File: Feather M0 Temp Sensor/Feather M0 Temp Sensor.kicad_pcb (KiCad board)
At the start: 2 copper layers, 35.6 x 22.9 mm, 3 parts, among them J1 Feather_Long_Side, J2 Feather_Short_Side, U1 Adafruit_SHT4x

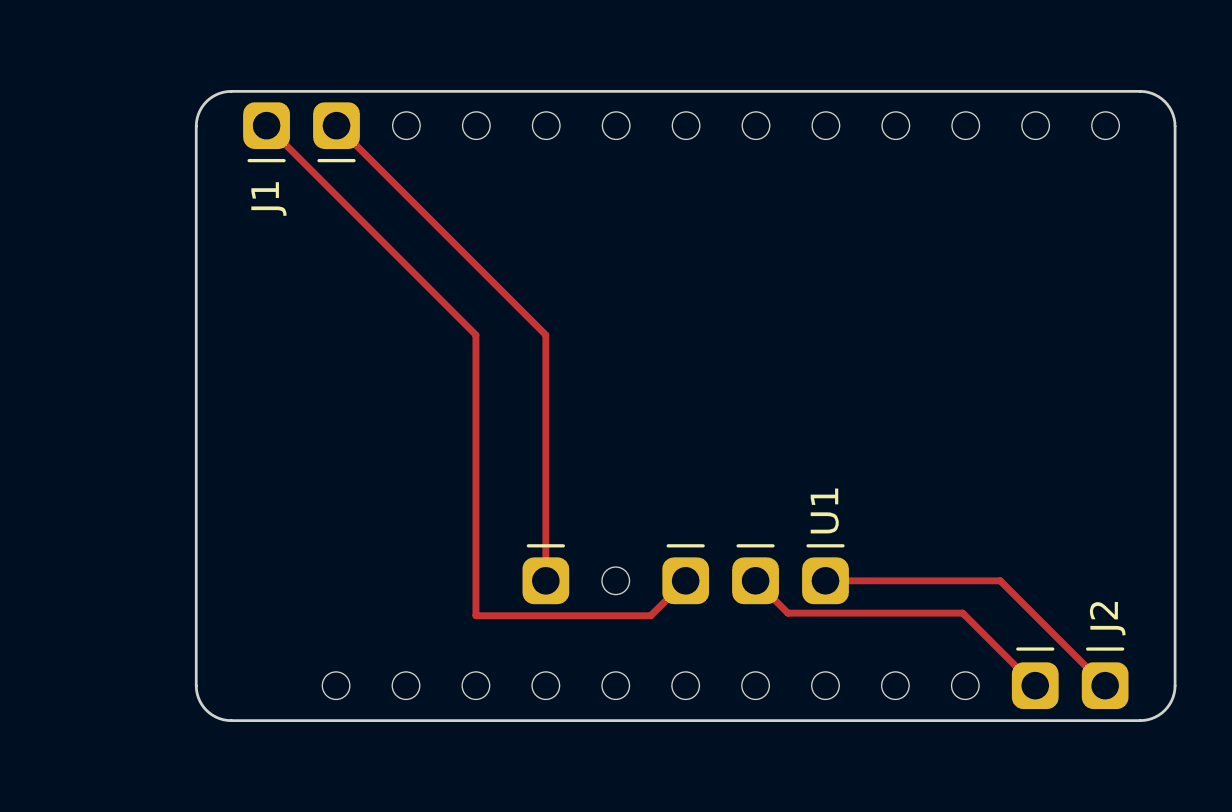
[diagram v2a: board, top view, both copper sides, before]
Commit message: Finalised PCB
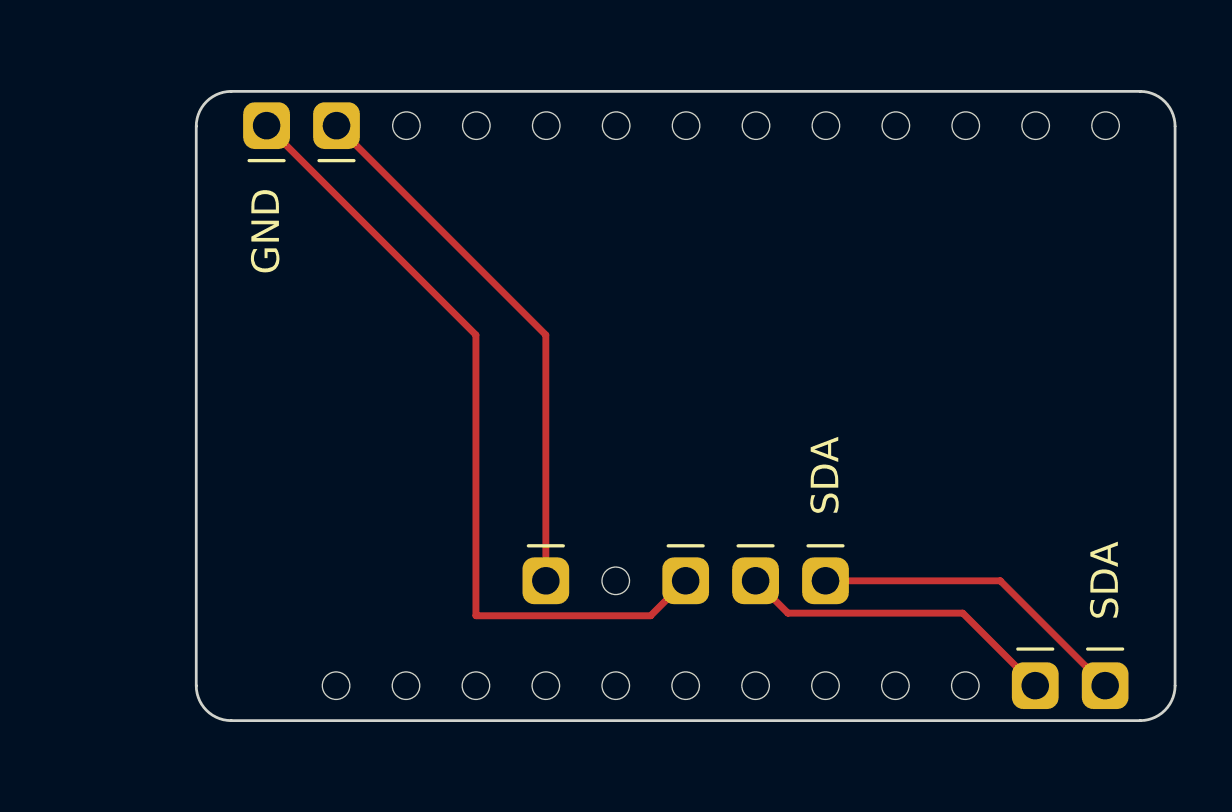
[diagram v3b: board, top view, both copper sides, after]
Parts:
- renumbered J1 to GND, U1 to SDA, J2 to SDA
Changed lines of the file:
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@@
     (property "Sheetname" "")
     (attr through_hole)
-    (fp_text reference "J1" (at -2.565 -0.015 90) (layer "F.SilkS")
+    (fp_text reference "GND" (at -3.835 -0.015 90) (layer "F.SilkS")
       (effects (font (size 1 1) (thickness 0.15)))
     )
@@
     (fp_line (start 1.75 32.25) (end -1.8 32.25) (layer "F.CrtYd") (width 0.05))
     (fp_line (start 1.75 -1.8) (end 1.75 32.25) (layer "F.CrtYd") (width 0.05))
+    (pad "" thru_hole oval (at 0 25.4 90) (size 1.7 1.7) (drill 1) (layers *.Mask)
+      (pinfunction "Pin_11") (pintype "passive"))
+    (pad "" thru_hole oval (at 0 15.24 90) (size 1.7 1.7) (drill 1) (layers *.Mask)
+      (pinfunction "Pin_7") (pintype "passive"))
+    (pad "" thru_hole oval (at 0 27.94 90) (size 1.7 1.7) (drill 1) (layers *.Mask)
+      (pinfunction "Pin_12") (pintype "passive"))
+    (pad "" thru_hole oval (at 0 30.48 90) (size 1.7 1.7) (drill 1) (layers *.Mask)
+      (pinfunction "Pin_13") (pintype "passive"))
+    (pad "" thru_hole oval (at 0 12.7 90) (size 1.7 1.7) (drill 1) (layers *.Mask)
+      (pinfunction "Pin_6") (pintype "passive"))
+    (pad "" thru_hole oval (at 0 22.86 90) (size 1.7 1.7) (drill 1) (layers *.Mask)
+      (pinfunction "Pin_10") (pintype "passive"))
+    (pad "" thru_hole oval (at 0 5.08 90) (size 1.7 1.7) (drill 1) (layers *.Mask)
+      (pinfunction "Pin_3") (pintype "passive"))
+    (pad "" thru_hole oval (at 0 7.62 90) (size 1.7 1.7) (drill 1) (layers *.Mask)
+      (pinfunction "Pin_4") (pintype "passive"))
+    (pad "" thru_hole oval (at 0 17.78 90) (size 1.7 1.7) (drill 1) (layers *.Mask)
+      (pinfunction "Pin_8") (pintype "passive"))
+    (pad "" thru_hole oval (at 0 20.32 90) (size 1.7 1.7) (drill 1) (layers *.Mask)
+      (pinfunction "Pin_9") (pintype "passive"))
+    (pad "" thru_hole oval (at 0 10.16 90) (size 1.7 1.7) (drill 1) (layers *.Mask)
+      (pinfunction "Pin_5") (pintype "passive"))
     (pad "1" thru_hole roundrect (at 0 0 90) (size 1.7 1.7) (drill 1) (layers *.Cu *.Mask) (roundrect_rratio 0.25)
       (net 2 "Net-(U1-Pad3)") (pinfunction "GND") (pintype "power_out"))
     (pad "2" thru_hole roundrect (at 0 2.54 90) (size 1.7 1.7) (drill 1) (layers *.Cu *.Mask) (roundrect_rratio 0.25)
       (net 3 "Net-(U1-Pad5)") (pinfunction "A0") (pintype "power_out"))
-    (pad "3" thru_hole oval (at 0 5.08 90) (size 1.7 1.7) (drill 1) (layers *.Mask)
-      (pinfunction "Pin_3") (pintype "passive"))
-    (pad "4" thru_hole oval (at 0 7.62 90) (size 1.7 1.7) (drill 1) (layers *.Mask)
-      (pinfunction "Pin_4") (pintype "passive"))
-    (pad "5" thru_hole oval (at 0 10.16 90) (size 1.7 1.7) (drill 1) (layers *.Mask)
-      (pinfunction "Pin_5") (pintype "passive"))
-    (pad "6" thru_hole oval (at 0 12.7 90) (size 1.7 1.7) (drill 1) (layers *.Mask)
-      (pinfunction "Pin_6") (pintype "passive"))
-    (pad "7" thru_hole oval (at 0 15.24 90) (size 1.7 1.7) (drill 1) (layers *.Mask)
-      (pinfunction "Pin_7") (pintype "passive"))
-    (pad "8" thru_hole oval (at 0 17.78 90) (size 1.7 1.7) (drill 1) (layers *.Mask)
-      (pinfunction "Pin_8") (pintype "passive"))
-    (pad "9" thru_hole oval (at 0 20.32 90) (size 1.7 1.7) (drill 1) (layers *.Mask)
-      (pinfunction "Pin_9") (pintype "passive"))
-    (pad "10" thru_hole oval (at 0 22.86 90) (size 1.7 1.7) (drill 1) (layers *.Mask)
-      (pinfunction "Pin_10") (pintype "passive"))
-    (pad "11" thru_hole oval (at 0 25.4 90) (size 1.7 1.7) (drill 1) (layers *.Mask)
-      (pinfunction "Pin_11") (pintype "passive"))
-    (pad "12" thru_hole oval (at 0 27.94 90) (size 1.7 1.7) (drill 1) (layers *.Mask)
-      (pinfunction "Pin_12") (pintype "passive"))
-    (pad "13" thru_hole oval (at 0 30.48 90) (size 1.7 1.7) (drill 1) (layers *.Mask)
-      (pinfunction "Pin_13") (pintype "passive"))
     (model "${KICAD6_3DMODEL_DIR}/Connector_PinSocket_2.54mm.3dshapes/PinSocket_1x13_P2.54mm_Vertical.wrl"
       (offset (xyz 0 0 0))
@@
     (property "Sheetname" "")
     (attr through_hole)
-    (fp_text reference "U1" (at -2.54 0 90) (layer "F.SilkS")
+    (fp_text reference "SDA" (at -3.81 0 90) (layer "F.SilkS")
       (effects (font (size 1 1) (thickness 0.15)))
     )
@@
     (fp_line (start 1.75 11.9) (end -1.8 11.9) (layer "F.CrtYd") (width 0.05))
     (fp_line (start -1.8 -1.8) (end 1.75 -1.8) (layer "F.CrtYd") (width 0.05))
+    (pad "" thru_hole oval (at 0 7.62 270) (size 1.7 1.7) (drill 1) (layers *.Mask)
+      (pinfunction "3V") (pintype "power_out"))
     (pad "1" thru_hole roundrect (at 0 0 270) (size 1.7 1.7) (drill 1) (layers *.Cu *.Mask) (roundrect_rratio 0.25)
       (net 1 "Net-(J2-Pad1)") (pinfunction "SDA") (pintype "bidirectional"))
@@
     (pad "3" thru_hole roundrect (at 0 5.08 270) (size 1.7 1.7) (drill 1) (layers *.Cu *.Mask) (roundrect_rratio 0.25)
       (net 2 "Net-(U1-Pad3)") (pinfunction "GND") (pintype "power_in"))
-    (pad "4" thru_hole oval (at 0 7.62 270) (size 1.7 1.7) (drill 1) (layers *.Mask)
-      (pinfunction "3V") (pintype "power_out"))
     (pad "5" thru_hole roundrect (at 0 10.16 270) (size 1.7 1.7) (drill 1) (layers *.Cu *.Mask) (roundrect_rratio 0.25)
       (net 3 "Net-(U1-Pad5)") (pinfunction "VIN") (pintype "power_in"))
@@
     (property "Sheetname" "")
     (attr through_hole)
-    (fp_text reference "J2" (at -2.54 0 90) (layer "F.SilkS")
+    (fp_text reference "SDA" (at -3.81 0 90) (layer "F.SilkS")
       (effects (font (size 1 1) (thickness 0.15)))
     )
@@
     (fp_line (start 1.75 -1.8) (end 1.75 29.7) (layer "F.CrtYd") (width 0.05))
     (fp_line (start 1.75 29.7) (end -1.8 29.7) (layer "F.CrtYd") (width 0.05))
+    (pad "" thru_hole oval (at 0 17.78 270) (size 1.7 1.7) (drill 1) (layers *.Mask)
+      (pinfunction "Pin_8") (pintype "passive"))
+    (pad "" thru_hole oval (at 0 7.62 270) (size 1.7 1.7) (drill 1) (layers *.Mask)
+      (pinfunction "Pin_4") (pintype "passive"))
+    (pad "" thru_hole oval (at 0 10.16 270) (size 1.7 1.7) (drill 1) (layers *.Mask)
+      (pinfunction "Pin_5") (pintype "passive"))
+    (pad "" thru_hole oval (at 0 5.08 270) (size 1.7 1.7) (drill 1) (layers *.Mask)
+      (pinfunction "Pin_3") (pintype "passive"))
+    (pad "" thru_hole oval (at 0 12.7 270) (size 1.7 1.7) (drill 1) (layers *.Mask)
+      (pinfunction "Pin_6") (pintype "passive"))
+    (pad "" thru_hole oval (at 0 20.32 270) (size 1.7 1.7) (drill 1) (layers *.Mask)
+      (pinfunction "Pin_9") (pintype "passive"))
+    (pad "" thru_hole oval (at 0 25.4 270) (size 1.7 1.7) (drill 1) (layers *.Mask)
+      (pinfunction "Pin_11") (pintype "passive"))
+    (pad "" thru_hole oval (at 0 15.24 270) (size 1.7 1.7) (drill 1) (layers *.Mask)
+      (pinfunction "Pin_7") (pintype "passive"))
+    (pad "" thru_hole oval (at 0 22.86 270) (size 1.7 1.7) (drill 1) (layers *.Mask)
+      (pinfunction "Pin_10") (pintype "passive"))
+    (pad "" thru_hole oval (at 0 27.94 270) (size 1.7 1.7) (drill 1) (layers *.Mask)
+      (pinfunction "Pin_12") (pintype "passive"))
     (pad "1" thru_hole roundrect (at 0 0 270) (size 1.7 1.7) (drill 1) (layers *.Cu *.Mask) (roundrect_rratio 0.25)
       (net 1 "Net-(J2-Pad1)") (pinfunction "SDA") (pintype "bidirectional"))
     (pad "2" thru_hole roundrect (at 0 2.54 270) (size 1.7 1.7) (drill 1) (layers *.Cu *.Mask) (roundrect_rratio 0.25)
       (net 4 "Net-(J2-Pad2)") (pinfunction "SCL") (pintype "output"))
-    (pad "3" thru_hole oval (at 0 5.08 270) (size 1.7 1.7) (drill 1) (layers *.Mask)
-      (pinfunction "Pin_3") (pintype "passive"))
-    (pad "4" thru_hole oval (at 0 7.62 270) (size 1.7 1.7) (drill 1) (layers *.Mask)
-      (pinfunction "Pin_4") (pintype "passive"))
-    (pad "5" thru_hole oval (at 0 10.16 270) (size 1.7 1.7) (drill 1) (layers *.Mask)
-      (pinfunction "Pin_5") (pintype "passive"))
-    (pad "6" thru_hole oval (at 0 12.7 270) (size 1.7 1.7) (drill 1) (layers *.Mask)
-      (pinfunction "Pin_6") (pintype "passive"))
-    (pad "7" thru_hole oval (at 0 15.24 270) (size 1.7 1.7) (drill 1) (layers *.Mask)
-      (pinfunction "Pin_7") (pintype "passive"))
-    (pad "8" thru_hole oval (at 0 17.78 270) (size 1.7 1.7) (drill 1) (layers *.Mask)
-      (pinfunction "Pin_8") (pintype "passive"))
-    (pad "9" thru_hole oval (at 0 20.32 270) (size 1.7 1.7) (drill 1) (layers *.Mask)
-      (pinfunction "Pin_9") (pintype "passive"))
-    (pad "10" thru_hole oval (at 0 22.86 270) (size 1.7 1.7) (drill 1) (layers *.Mask)
-      (pinfunction "Pin_10") (pintype "passive"))
-    (pad "11" thru_hole oval (at 0 25.4 270) (size 1.7 1.7) (drill 1) (layers *.Mask)
-      (pinfunction "Pin_11") (pintype "passive"))
-    (pad "12" thru_hole oval (at 0 27.94 270) (size 1.7 1.7) (drill 1) (layers *.Mask)
-      (pinfunction "Pin_12") (pintype "passive"))
     (model "${KICAD6_3DMODEL_DIR}/Connector_PinSocket_2.54mm.3dshapes/PinSocket_1x12_P2.54mm_Vertical.wrl"
       (offset (xyz 0 0 0))
